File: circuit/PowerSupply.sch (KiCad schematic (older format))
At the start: 16 parts, among them CN1 Battery, CN2 Battery, Q1 IRLML6402, SW1 SW_SPDT, U1 NJM7805S, U2 LM3940IMP-3.3

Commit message: あってぃ！
今月中にElecrow発注したいんじゃ〜〜〜
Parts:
- D1: value PWR_LED -> PWR_LED(Red); footprint (none) -> LEDs:LED_0603
- R1: value 100k -> 100k 0.25W; footprint (none) -> Resistors_SMD:R_0603
- R2: value 10k -> 20k; footprint (none) -> Resistors_SMD:R_0805
- R3: value 2.7k -> 10k; footprint (none) -> Resistors_SMD:R_0805
- R4: footprint (none) -> Resistors_SMD:R_0603
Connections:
- net labels removed: +3V3
- wire segments 69 -> 64
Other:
- note added: "I = 2.8 / 10k \n = 0.28mA\nWu = 0.1568 W < 1/4 W\nWd = 0.0784 W < 1/4 W"
- note added: "Imax = 1.5A\n"
- note added: "Imax = 1A"
- note added: "R = (5 - 1.9)/0.005 = 620"
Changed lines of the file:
@@
 P 2400 1800
 F 0 "R1" H 2470 1846 50  0000 L CNN
-F 1 "100k" H 2470 1755 50  0000 L CNN
-F 2 "" V 2330 1800 50  0001 C CNN
+F 1 "100k 0.25W" H 2470 1755 50  0000 L CNN
+F 2 "Resistors_SMD:R_0603" V 2330 1800 50  0001 C CNN
 F 3 "" H 2400 1800 50  0001 C CNN
 	1    2400 1800
@@
 P 4750 1950
 F 0 "D1" V 4789 1833 50  0000 R CNN
-F 1 "PWR_LED" V 4698 1833 50  0000 R CNN
-F 2 "" H 4750 1950 50  0001 C CNN
-F 3 "" H 4750 1950 50  0001 C CNN
+F 1 "PWR_LED(Red)" V 4698 1833 50  0000 R CNN
+F 2 "LEDs:LED_0603" H 4750 1950 50  0001 C CNN
+F 3 "https://akizukidenshi.com/download/ds/optosupply/OSXX1608C1A_ver_a_10.pdf" H 4750 1950 50  0001 C CNN
 	1    4750 1950
 	0    -1   -1   0
@@
 F 0 "R4" H 4820 1596 50  0000 L CNN
 F 1 "1k" H 4820 1505 50  0000 L CNN
-F 2 "" V 4680 1550 50  0001 C CNN
+F 2 "Resistors_SMD:R_0603" V 4680 1550 50  0001 C CNN
 F 3 "" H 4750 1550 50  0001 C CNN
 	1    4750 1550
@@
 P 3150 3800
 F 0 "R2" H 3220 3846 50  0000 L CNN
-F 1 "10k" H 3220 3755 50  0000 L CNN
-F 2 "" V 3080 3800 50  0001 C CNN
+F 1 "20k" H 3220 3755 50  0000 L CNN
+F 2 "Resistors_SMD:R_0805" V 3080 3800 50  0001 C CNN
 F 3 "" H 3150 3800 50  0001 C CNN
 	1    3150 3800
@@
 P 3150 4300
 F 0 "R3" H 3220 4346 50  0000 L CNN
-F 1 "2.7k" H 3220 4255 50  0000 L CNN
-F 2 "" V 3080 4300 50  0001 C CNN
+F 1 "10k" H 3220 4255 50  0000 L CNN
+F 2 "Resistors_SMD:R_0805" V 3080 4300 50  0001 C CNN
 F 3 "" H 3150 4300 50  0001 C CNN
 	1    3150 4300
@@
 Wire Wire Line
 	3150 4050 3150 4150
-Text Notes 3450 3800 0    50   ~ 0
+Text Notes 3450 3550 0    50   ~ 0
 VCC=8.4V\nSEN_BAT=8.4 * 10k / (10k+20k)\n = 2.8V
 $Comp
@@
 	1    0    0    -1
 $EndComp
-$Comp
-L power:+5V #PWR0113
-U 1 1 5F96E56A
-P 2150 3500
-F 0 "#PWR0113" H 2150 3350 50  0001 C CNN
-F 1 "+5V" H 2165 3673 50  0000 C CNN
-F 2 "" H 2150 3500 50  0001 C CNN
-F 3 "" H 2150 3500 50  0001 C CNN
-	1    2150 3500
-	1    0    0    -1
-$EndComp
 Wire Wire Line
 	1150 3600 1150 3500
@@
 Wire Wire Line
 	1800 3600 1800 3500
-Wire Wire Line
-	2150 3500 2150 3600
 $Comp
 L regul:LM3940IMP-3.3 U2
@@
 L power:GND #PWR0114
 U 1 1 5F98E5D7
-P 6500 2250
-F 0 "#PWR0114" H 6500 2000 50  0001 C CNN
-F 1 "GND" H 6505 2077 50  0000 C CNN
-F 2 "" H 6500 2250 50  0001 C CNN
-F 3 "" H 6500 2250 50  0001 C CNN
-	1    6500 2250
+P 6500 2400
+F 0 "#PWR0114" H 6500 2150 50  0001 C CNN
+F 1 "GND" H 6505 2227 50  0000 C CNN
+F 2 "" H 6500 2400 50  0001 C CNN
+F 3 "" H 6500 2400 50  0001 C CNN
+	1    6500 2400
 	1    0    0    -1
 $EndComp
@@
 	7700 1250 7200 1250
 Connection ~ 7200 1250
-$Comp
-L power:+3V3 #PWR0116
-U 1 1 5F9A92FF
-P 1450 3950
-F 0 "#PWR0116" H 1450 3800 50  0001 C CNN
-F 1 "+3V3" H 1465 4123 50  0000 C CNN
-F 2 "" H 1450 3950 50  0001 C CNN
-F 3 "" H 1450 3950 50  0001 C CNN
-	1    1450 3950
-	1    0    0    -1
-$EndComp
-$Comp
-L power:PWR_FLAG #FLG0105
-U 1 1 5F9A9842
-P 1800 3950
-F 0 "#FLG0105" H 1800 4025 50  0001 C CNN
-F 1 "PWR_FLAG" H 1800 4123 50  0000 C CNN
-F 2 "" H 1800 3950 50  0001 C CNN
-F 3 "" H 1800 3950 50  0001 C CNN
-	1    1800 3950
-	1    0    0    -1
-$EndComp
-Wire Wire Line
-	1450 3950 1450 4100
-Wire Wire Line
-	1450 4100 1800 4100
-Wire Wire Line
-	1800 4100 1800 3950
 NoConn ~ 2500 2400
-$Comp
-L power:PWR_FLAG #FLG0104
-U 1 1 5F9823F2
-P 2500 3500
-F 0 "#FLG0104" H 2500 3575 50  0001 C CNN
-F 1 "PWR_FLAG" H 2500 3673 50  0000 C CNN
-F 2 "" H 2500 3500 50  0001 C CNN
-F 3 "" H 2500 3500 50  0001 C CNN
-	1    2500 3500
-	1    0    0    -1
-$EndComp
-Wire Wire Line
-	2150 3600 2500 3600
-Wire Wire Line
-	2500 3600 2500 3500
 Wire Wire Line
 	2750 1000 2750 1250
 $Comp
-L power:+3.3V #PWR?
+L power:+3.3V #PWR0131
 U 1 1 5F9CE132
 P 7700 1000
-F 0 "#PWR?" H 7700 850 50  0001 C CNN
+F 0 "#PWR0131" H 7700 850 50  0001 C CNN
 F 1 "+3.3V" H 7715 1173 50  0000 C CNN
 F 2 "" H 7700 1000 50  0001 C CNN
@@
 Text HLabel 3750 4050 2    50   Input ~ 0
 BAT_MONI
+Text Notes 3900 1100 0    50   ~ 0
+Imax = 1.5A\n
+Text Notes 6650 1000 0    50   ~ 0
+Imax = 1A
+Wire Wire Line
+	6500 2250 6500 2400
+Text Notes 4300 2550 0    50   ~ 0
+R = (5 - 1.9)/0.005 = 620
+Text Notes 2050 4150 0    50   ~ 0
+I = 2.8 / 10k \n  = 0.28mA\nWu = 0.1568 W < 1/4 W\nWd = 0.0784 W < 1/4 W
 $EndSCHEMATC

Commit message: Kicad v5.1.8対応
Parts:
- removed C5: 33uF, symbol device:C
- removed U2: LM3940IMP-3.3, TO_SOT_Packages_SMD:SOT-223, symbol regul:LM3940IMP-3.3
- added C24: 2.2u, symbol Device:C
- added U4: ADP7182AUJZ-3.3, Package_TO_SOT_SMD:TSOT-23-5, symbol Regulator_Linear:ADP7182AUJZ-3.3
- C1: value 0.33uF -> 4.7u; footprint (none) -> Capacitors_SMD:C_0805; symbol device:C -> Device:C
- C2: symbol device:C -> Device:C
- C3: value 0.1uF -> 1u; footprint (none) -> Capacitors_SMD:C_0603; symbol device:C -> Device:C
- C4: value 0.47uF -> 2.2u; symbol device:C -> Device:C
- CN1, CN2: symbol conn:Conn_01x02 -> Connector_Generic:Conn_01x02
- D1: symbol device:LED -> Device:LED
- Q1: symbol device:Q_PMOS_GSD -> Device:Q_PMOS_GSD
- R1, R2, R3, R4: symbol device:R -> Device:R
- SW1: symbol switches:SW_SPDT -> Switch:SW_SPDT
- U1: symbol regul:NJM7805S -> Regulator_Linear:NJM7805S
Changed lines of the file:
@@
 $EndComp
 $Comp
-L device:R R1
+L Device:R R1
 U 1 1 5F95E89C
 P 2400 1800
@@
 $EndComp
 $Comp
-L conn:Conn_01x02 CN1
+L Connector_Generic:Conn_01x02 CN1
 U 1 1 5F9556B5
 P 1000 1350
+AR Path="/5F9556B5" Ref="CN1"  Part="1"
+AR Path="/5F951566/5F9556B5" Ref="CN1"  Part="1"
 F 0 "CN1" H 1000 1000 50  0000 C CNN
 F 1 "Battery" H 1000 1100 50  0000 C CNN
@@
 Connection ~ 1750 1250
 $Comp
-L conn:Conn_01x02 CN2
+L Connector_Generic:Conn_01x02 CN2
 U 1 1 5F93F701
 P 1000 1900
+AR Path="/5F93F701" Ref="CN2"  Part="1"
+AR Path="/5F951566/5F93F701" Ref="CN2"  Part="1"
 F 0 "CN2" H 1000 1550 50  0000 C CNN
 F 1 "Battery" H 1000 1650 50  0000 C CNN
@@
 $EndComp
 $Comp
-L device:Q_PMOS_GSD Q1
+L Device:Q_PMOS_GSD Q1
 U 1 1 5F95A78B
 P 2400 1350
@@
 Connection ~ 2400 1600
 $Comp
-L switches:SW_SPDT SW1
+L Switch:SW_SPDT SW1
 U 1 1 5F987A18
 P 2400 2200
@@
 	2400 2000 2400 1950
 $Comp
-L device:LED D1
+L Device:LED D1
 U 1 1 5F94B7CC
 P 4750 1950
@@
 	4750 2100 4750 2200
 $Comp
-L regul:NJM7805S U1
-U 1 1 5F93E0A1
-P 3600 1250
-F 0 "U1" H 3600 1565 50  0000 C CNN
-F 1 "NJM7805S" H 3600 1474 50  0000 C CNN
-F 2 "TO_SOT_Packages_SMD:TO-252-2" H 3600 1700 50  0001 C CNN
-F 3 "https://akizukidenshi.com/download/ds/njr/NJM7800S_J.pdf" H 3650 950 50  0001 C CNN
-	1    3600 1250
-	1    0    0    -1
-$EndComp
-$Comp
 L power:GND #PWR0106
 U 1 1 5F9424A0
@@
 Wire Wire Line
 	3600 1600 3600 1750
-$Comp
-L device:C C1
-U 1 1 5F942D36
-P 3100 1550
-F 0 "C1" H 3215 1596 50  0000 L CNN
-F 1 "0.33uF" H 3215 1505 50  0000 L CNN
-F 2 "" H 3138 1400 50  0001 C CNN
-F 3 "" H 3100 1550 50  0001 C CNN
-	1    3100 1550
-	1    0    0    -1
-$EndComp
 Wire Wire Line
 	2750 1250 3100 1250
@@
 Wire Wire Line
 	3600 1750 3600 1800
-$Comp
-L device:C C3
-U 1 1 5F943C3B
-P 4100 1550
-F 0 "C3" H 4215 1596 50  0000 L CNN
-F 1 "0.1uF" H 4215 1505 50  0000 L CNN
-F 2 "" H 4138 1400 50  0001 C CNN
-F 3 "" H 4100 1550 50  0001 C CNN
-	1    4100 1550
-	1    0    0    -1
-$EndComp
 Wire Wire Line
 	3600 1750 4100 1750
@@
 	4100 1250 4100 1400
 $Comp
-L device:R R4
+L Device:R R4
 U 1 1 5F945E92
 P 4750 1550
@@
 $EndComp
 $Comp
-L device:R R2
+L Device:R R2
 U 1 1 5F95A42B
 P 3150 3800
@@
 $EndComp
 $Comp
-L device:R R3
+L Device:R R3
 U 1 1 5F95A966
 P 3150 4300
@@
 VCC=8.4V\nSEN_BAT=8.4 * 10k / (10k+20k)\n = 2.8V
 $Comp
-L device:C C2
+L Device:C C2
 U 1 1 5F95E36D
 P 3550 4300
@@
 	1800 3600 1800 3500
 $Comp
-L regul:LM3940IMP-3.3 U2
-U 1 1 5F98DB71
-P 6500 1350
-F 0 "U2" H 6500 1715 50  0000 C CNN
-F 1 "LM3940IMP-3.3" H 6500 1624 50  0000 C CNN
-F 2 "TO_SOT_Packages_SMD:SOT-223" H 6500 1700 50  0001 C CNN
-F 3 "https://www.ti.com/lit/ds/symlink/lm3940.pdf?HQS=TI-null-null-digikeymode-df-pf-null-wwe&ts=1603528827635" H 6500 1700 50  0001 C CNN
-	1    6500 1350
-	1    0    0    -1
-$EndComp
-$Comp
 L power:GND #PWR0114
 U 1 1 5F98E5D7
-P 6500 2400
-F 0 "#PWR0114" H 6500 2150 50  0001 C CNN
-F 1 "GND" H 6505 2227 50  0000 C CNN
-F 2 "" H 6500 2400 50  0001 C CNN
-F 3 "" H 6500 2400 50  0001 C CNN
-	1    6500 2400
-	1    0    0    -1
-$EndComp
-Wire Wire Line
-	6000 1450 6000 2250
-Wire Wire Line
-	6000 2250 6500 2250
-Wire Wire Line
-	7000 1450 7000 2250
-Wire Wire Line
-	7000 2250 6500 2250
-Connection ~ 6500 2250
-Wire Wire Line
-	6000 1250 5600 1250
-$Comp
-L device:C C4
-U 1 1 5F992186
-P 5600 1800
-F 0 "C4" H 5715 1846 50  0000 L CNN
-F 1 "0.47uF" H 5715 1755 50  0000 L CNN
-F 2 "" H 5638 1650 50  0001 C CNN
-F 3 "" H 5600 1800 50  0001 C CNN
-	1    5600 1800
-	1    0    0    -1
-$EndComp
-Wire Wire Line
-	5600 1250 5600 1650
-Connection ~ 5600 1250
-Wire Wire Line
-	5600 1250 4750 1250
-Wire Wire Line
-	5600 1950 5600 2250
-Wire Wire Line
-	5600 2250 6000 2250
-Connection ~ 6000 2250
-$Comp
-L device:C C5
-U 1 1 5F99CDC1
-P 7200 1800
-F 0 "C5" H 7315 1846 50  0000 L CNN
-F 1 "33uF" H 7315 1755 50  0000 L CNN
-F 2 "" H 7238 1650 50  0001 C CNN
-F 3 "" H 7200 1800 50  0001 C CNN
-	1    7200 1800
-	1    0    0    -1
-$EndComp
-Wire Wire Line
-	7200 1950 7200 2250
-Wire Wire Line
-	7200 2250 7000 2250
-Connection ~ 7000 2250
-Wire Wire Line
-	7000 1250 7200 1250
-Wire Wire Line
-	7200 1250 7200 1650
+P 6500 2250
+F 0 "#PWR0114" H 6500 2000 50  0001 C CNN
+F 1 "GND" H 6505 2077 50  0000 C CNN
+F 2 "" H 6500 2250 50  0001 C CNN
+F 3 "" H 6500 2250 50  0001 C CNN
+	1    6500 2250
+	1    0    0    -1
+$EndComp
+Connection ~ 6500 2100
+Wire Wire Line
+	5850 1250 5850 1650
+Connection ~ 5850 1250
+Wire Wire Line
+	5850 1250 4750 1250
+Wire Wire Line
+	5850 1950 5850 2100
+Wire Wire Line
+	6950 1250 6950 1650
 Wire Wire Line
 	7700 1000 7700 1250
 Wire Wire Line
-	7700 1250 7200 1250
-Connection ~ 7200 1250
+	7700 1250 6950 1250
+Connection ~ 6950 1250
 NoConn ~ 2500 2400
 Wire Wire Line
@@
 Imax = 1A
 Wire Wire Line
-	6500 2250 6500 2400
+	6500 2100 6500 2250
 Text Notes 4300 2550 0    50   ~ 0
 R = (5 - 1.9)/0.005 = 620
 Text Notes 2050 4150 0    50   ~ 0
 I = 2.8 / 10k \n  = 0.28mA\nWu = 0.1568 W < 1/4 W\nWd = 0.0784 W < 1/4 W
+$Comp
+L Device:C C4
+U 1 1 5F992186
+P 5850 1800
+F 0 "C4" H 5965 1846 50  0000 L CNN
+F 1 "2.2u" H 5965 1755 50  0000 L CNN
+F 2 "" H 5888 1650 50  0001 C CNN
+F 3 "" H 5850 1800 50  0001 C CNN
+	1    5850 1800
+	1    0    0    -1
+$EndComp
+$Comp
+L Device:C C1
+U 1 1 5F942D36
+P 3100 1550
+F 0 "C1" H 3215 1596 50  0000 L CNN
+F 1 "4.7u" H 3215 1505 50  0000 L CNN
+F 2 "Capacitors_SMD:C_0805" H 3138 1400 50  0001 C CNN
+F 3 "" H 3100 1550 50  0001 C CNN
+	1    3100 1550
+	1    0    0    -1
+$EndComp
+$Comp
+L Regulator_Linear:NJM7805S U1
+U 1 1 5F93E0A1
+P 3600 1250
+F 0 "U1" H 3600 1565 50  0000 C CNN
+F 1 "NJM7805S" H 3600 1474 50  0000 C CNN
+F 2 "TO_SOT_Packages_SMD:TO-252-2" H 3600 1700 50  0001 C CNN
+F 3 "https://akizukidenshi.com/download/ds/njr/NJM7800S_J.pdf" H 3650 950 50  0001 C CNN
+	1    3600 1250
+	1    0    0    -1
+$EndComp
+$Comp
+L Device:C C3
+U 1 1 5F943C3B
+P 4100 1550
+F 0 "C3" H 4215 1596 50  0000 L CNN
+F 1 "1u" H 4215 1505 50  0000 L CNN
+F 2 "Capacitors_SMD:C_0603" H 4138 1400 50  0001 C CNN
+F 3 "" H 4100 1550 50  0001 C CNN
+	1    4100 1550
+	1    0    0    -1
+$EndComp
+Wire Wire Line
+	5850 2100 6500 2100
+Wire Wire Line
+	6500 2100 6950 2100
+$Comp
+L Regulator_Linear:ADP7182AUJZ-3.3 U4
+U 1 1 5FB8CF9C
+P 6500 1350
+F 0 "U4" H 6500 983 50  0000 C CNN
+F 1 "ADP7182AUJZ-3.3" H 6500 1074 50  0000 C CNN
+F 2 "Package_TO_SOT_SMD:TSOT-23-5" H 6500 950 50  0001 C CIN
+F 3 "https://www.analog.com/media/en/technical-documentation/data-sheets/ADP7182.pdf" H 6500 850 50  0001 C CNN
+	1    6500 1350
+	1    0    0    1
+$EndComp
+Wire Wire Line
+	5850 1250 6000 1250
+Wire Wire Line
+	6900 1250 6950 1250
+Wire Wire Line
+	6100 1450 6000 1450
+Wire Wire Line
+	6000 1450 6000 1250
+Connection ~ 6000 1250
+Wire Wire Line
+	6000 1250 6100 1250
+Wire Wire Line
+	6500 1650 6500 2100
+$Comp
+L Device:C C24
+U 1 1 5FBA0D44
+P 6950 1800
+F 0 "C24" H 7065 1846 50  0000 L CNN
+F 1 "2.2u" H 7065 1755 50  0000 L CNN
+F 2 "" H 6988 1650 50  0001 C CNN
+F 3 "" H 6950 1800 50  0001 C CNN
+	1    6950 1800
+	1    0    0    -1
+$EndComp
+Wire Wire Line
+	6950 1950 6950 2100
 $EndSCHEMATC

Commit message: Kicadのpcbnew映らないくてキレそう
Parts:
- C2, C24, C4: footprint (none) -> Capacitors_SMD:C_0603
- CN1, CN2: footprint (none) -> Connectors_JST:JST_PH_B2B-PH-K_02x2.00mm_Straight
- Q1: footprint (none) -> TO_SOT_Packages_SMD:SOT-23
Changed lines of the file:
@@
 F 0 "CN1" H 1000 1000 50  0000 C CNN
 F 1 "Battery" H 1000 1100 50  0000 C CNN
-F 2 "" H 1000 1350 50  0001 C CNN
+F 2 "Connectors_JST:JST_PH_B2B-PH-K_02x2.00mm_Straight" H 1000 1350 50  0001 C CNN
 F 3 "~" H 1000 1350 50  0001 C CNN
 	1    1000 1350
@@
 F 0 "CN2" H 1000 1550 50  0000 C CNN
 F 1 "Battery" H 1000 1650 50  0000 C CNN
-F 2 "" H 1000 1900 50  0001 C CNN
+F 2 "Connectors_JST:JST_PH_B2B-PH-K_02x2.00mm_Straight" H 1000 1900 50  0001 C CNN
 F 3 "~" H 1000 1900 50  0001 C CNN
 	1    1000 1900
@@
 F 0 "Q1" H 2606 1396 50  0000 L CNN
 F 1 "IRLML6402" H 2606 1305 50  0000 L CNN
-F 2 "" H 2600 1450 50  0001 C CNN
-F 3 "" H 2400 1350 50  0001 C CNN
+F 2 "TO_SOT_Packages_SMD:SOT-23" H 2600 1450 50  0001 C CNN
+F 3 "https://akizukidenshi.com/download/ds/ir/irlml6402.pdf" H 2400 1350 50  0001 C CNN
 	1    2400 1350
 	0    1    -1   0
@@
 F 0 "C2" H 3665 4346 50  0000 L CNN
 F 1 "0.1uF" H 3665 4255 50  0000 L CNN
-F 2 "" H 3588 4150 50  0001 C CNN
+F 2 "Capacitors_SMD:C_0603" H 3588 4150 50  0001 C CNN
 F 3 "" H 3550 4300 50  0001 C CNN
 	1    3550 4300
@@
 F 0 "C4" H 5965 1846 50  0000 L CNN
 F 1 "2.2u" H 5965 1755 50  0000 L CNN
-F 2 "" H 5888 1650 50  0001 C CNN
+F 2 "Capacitors_SMD:C_0603" H 5888 1650 50  0001 C CNN
 F 3 "" H 5850 1800 50  0001 C CNN
 	1    5850 1800
@@
 F 0 "C24" H 7065 1846 50  0000 L CNN
 F 1 "2.2u" H 7065 1755 50  0000 L CNN
-F 2 "" H 6988 1650 50  0001 C CNN
+F 2 "Capacitors_SMD:C_0603" H 6988 1650 50  0001 C CNN
 F 3 "" H 6950 1800 50  0001 C CNN
 	1    6950 1800

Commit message: スーパーエンジニアの登竜門たる文彦は当然スーパーエンジニア
あってぃ許さない
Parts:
- C1: footprint Capacitors_SMD:C_0805 -> Capacitor_SMD:C_0805_2012Metric
- C2, C24, C3, C4: footprint Capacitors_SMD:C_0603 -> Capacitor_SMD:C_0603_1608Metric
- CN1, CN2: footprint Connectors_JST:JST_PH_B2B-PH-K_02x2.00mm_Straight -> Connector_JST:JST_PH_B2B-PH-K_1x02_P2.00mm_Vertical
- D1: footprint LEDs:LED_0603 -> LED_SMD:LED_0603_1608Metric
- Q1: footprint TO_SOT_Packages_SMD:SOT-23 -> Package_TO_SOT_SMD:SOT-23
- R1, R4: footprint Resistors_SMD:R_0603 -> Resistor_SMD:R_0603_1608Metric
- R2, R3: footprint Resistors_SMD:R_0805 -> Resistor_SMD:R_0805_2012Metric
- SW1: footprint (none) -> Button_Switch_THT:SW_CuK_JS202011CQN_DPDT_Straight
- U1: footprint TO_SOT_Packages_SMD:TO-252-2 -> Package_TO_SOT_SMD:TO-252-2; symbol Regulator_Linear:NJM7805S -> Micromouse-rescue:NJM7805S-Regulator_Linear
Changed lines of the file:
@@
 F 0 "R1" H 2470 1846 50  0000 L CNN
 F 1 "100k 0.25W" H 2470 1755 50  0000 L CNN
-F 2 "Resistors_SMD:R_0603" V 2330 1800 50  0001 C CNN
+F 2 "Resistor_SMD:R_0603_1608Metric" V 2330 1800 50  0001 C CNN
 F 3 "" H 2400 1800 50  0001 C CNN
 	1    2400 1800
@@
 F 0 "CN1" H 1000 1000 50  0000 C CNN
 F 1 "Battery" H 1000 1100 50  0000 C CNN
-F 2 "Connectors_JST:JST_PH_B2B-PH-K_02x2.00mm_Straight" H 1000 1350 50  0001 C CNN
+F 2 "Connector_JST:JST_PH_B2B-PH-K_1x02_P2.00mm_Vertical" H 1000 1350 50  0001 C CNN
 F 3 "~" H 1000 1350 50  0001 C CNN
 	1    1000 1350
@@
 F 0 "CN2" H 1000 1550 50  0000 C CNN
 F 1 "Battery" H 1000 1650 50  0000 C CNN
-F 2 "Connectors_JST:JST_PH_B2B-PH-K_02x2.00mm_Straight" H 1000 1900 50  0001 C CNN
+F 2 "Connector_JST:JST_PH_B2B-PH-K_1x02_P2.00mm_Vertical" H 1000 1900 50  0001 C CNN
 F 3 "~" H 1000 1900 50  0001 C CNN
 	1    1000 1900
@@
 F 0 "Q1" H 2606 1396 50  0000 L CNN
 F 1 "IRLML6402" H 2606 1305 50  0000 L CNN
-F 2 "TO_SOT_Packages_SMD:SOT-23" H 2600 1450 50  0001 C CNN
+F 2 "Package_TO_SOT_SMD:SOT-23" H 2600 1450 50  0001 C CNN
 F 3 "https://akizukidenshi.com/download/ds/ir/irlml6402.pdf" H 2400 1350 50  0001 C CNN
 	1    2400 1350
@@
 F 0 "SW1" V 2446 2012 50  0000 R CNN
 F 1 "SW_SPDT" V 2355 2012 50  0000 R CNN
-F 2 "" H 2400 2200 50  0001 C CNN
+F 2 "Button_Switch_THT:SW_CuK_JS202011CQN_DPDT_Straight" H 2400 2200 50  0001 C CNN
 F 3 "" H 2400 2200 50  0001 C CNN
 	1    2400 2200
@@
 F 0 "D1" V 4789 1833 50  0000 R CNN
 F 1 "PWR_LED(Red)" V 4698 1833 50  0000 R CNN
-F 2 "LEDs:LED_0603" H 4750 1950 50  0001 C CNN
+F 2 "LED_SMD:LED_0603_1608Metric" H 4750 1950 50  0001 C CNN
 F 3 "https://akizukidenshi.com/download/ds/optosupply/OSXX1608C1A_ver_a_10.pdf" H 4750 1950 50  0001 C CNN
 	1    4750 1950
@@
 F 0 "R4" H 4820 1596 50  0000 L CNN
 F 1 "1k" H 4820 1505 50  0000 L CNN
-F 2 "Resistors_SMD:R_0603" V 4680 1550 50  0001 C CNN
+F 2 "Resistor_SMD:R_0603_1608Metric" V 4680 1550 50  0001 C CNN
 F 3 "" H 4750 1550 50  0001 C CNN
 	1    4750 1550
@@
 F 0 "R2" H 3220 3846 50  0000 L CNN
 F 1 "20k" H 3220 3755 50  0000 L CNN
-F 2 "Resistors_SMD:R_0805" V 3080 3800 50  0001 C CNN
+F 2 "Resistor_SMD:R_0805_2012Metric" V 3080 3800 50  0001 C CNN
 F 3 "" H 3150 3800 50  0001 C CNN
 	1    3150 3800
@@
 F 0 "R3" H 3220 4346 50  0000 L CNN
 F 1 "10k" H 3220 4255 50  0000 L CNN
-F 2 "Resistors_SMD:R_0805" V 3080 4300 50  0001 C CNN
+F 2 "Resistor_SMD:R_0805_2012Metric" V 3080 4300 50  0001 C CNN
 F 3 "" H 3150 4300 50  0001 C CNN
 	1    3150 4300
@@
 F 0 "C2" H 3665 4346 50  0000 L CNN
 F 1 "0.1uF" H 3665 4255 50  0000 L CNN
-F 2 "Capacitors_SMD:C_0603" H 3588 4150 50  0001 C CNN
+F 2 "Capacitor_SMD:C_0603_1608Metric" H 3588 4150 50  0001 C CNN
 F 3 "" H 3550 4300 50  0001 C CNN
 	1    3550 4300
@@
 F 0 "C4" H 5965 1846 50  0000 L CNN
 F 1 "2.2u" H 5965 1755 50  0000 L CNN
-F 2 "Capacitors_SMD:C_0603" H 5888 1650 50  0001 C CNN
+F 2 "Capacitor_SMD:C_0603_1608Metric" H 5888 1650 50  0001 C CNN
 F 3 "" H 5850 1800 50  0001 C CNN
 	1    5850 1800
@@
 F 0 "C1" H 3215 1596 50  0000 L CNN
 F 1 "4.7u" H 3215 1505 50  0000 L CNN
-F 2 "Capacitors_SMD:C_0805" H 3138 1400 50  0001 C CNN
+F 2 "Capacitor_SMD:C_0805_2012Metric" H 3138 1400 50  0001 C CNN
 F 3 "" H 3100 1550 50  0001 C CNN
 	1    3100 1550
@@
 $EndComp
 $Comp
-L Regulator_Linear:NJM7805S U1
+L Micromouse-rescue:NJM7805S-Regulator_Linear U1
 U 1 1 5F93E0A1
 P 3600 1250
+AR Path="/5F93E0A1" Ref="U1"  Part="1"
+AR Path="/5F951566/5F93E0A1" Ref="U1"  Part="1"
 F 0 "U1" H 3600 1565 50  0000 C CNN
 F 1 "NJM7805S" H 3600 1474 50  0000 C CNN
-F 2 "TO_SOT_Packages_SMD:TO-252-2" H 3600 1700 50  0001 C CNN
+F 2 "Package_TO_SOT_SMD:TO-252-2" H 3600 1700 50  0001 C CNN
 F 3 "https://akizukidenshi.com/download/ds/njr/NJM7800S_J.pdf" H 3650 950 50  0001 C CNN
 	1    3600 1250
@@
 F 0 "C3" H 4215 1596 50  0000 L CNN
 F 1 "1u" H 4215 1505 50  0000 L CNN
-F 2 "Capacitors_SMD:C_0603" H 4138 1400 50  0001 C CNN
+F 2 "Capacitor_SMD:C_0603_1608Metric" H 4138 1400 50  0001 C CNN
 F 3 "" H 4100 1550 50  0001 C CNN
 	1    4100 1550
@@
 F 0 "C24" H 7065 1846 50  0000 L CNN
 F 1 "2.2u" H 7065 1755 50  0000 L CNN
-F 2 "Capacitors_SMD:C_0603" H 6988 1650 50  0001 C CNN
+F 2 "Capacitor_SMD:C_0603_1608Metric" H 6988 1650 50  0001 C CNN
 F 3 "" H 6950 1800 50  0001 C CNN
 	1    6950 1800

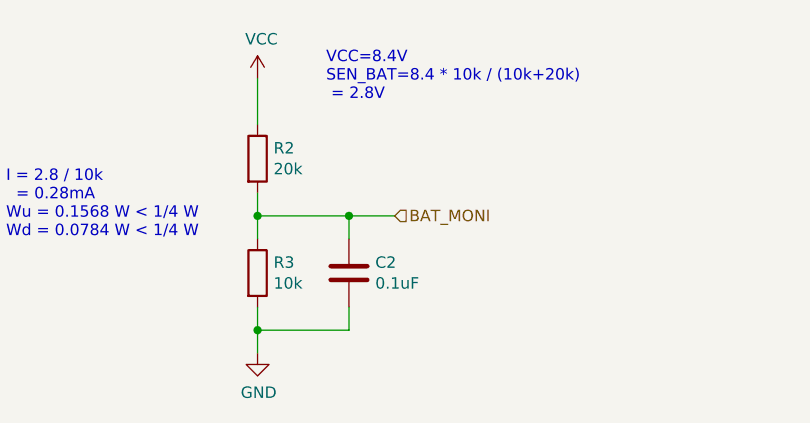
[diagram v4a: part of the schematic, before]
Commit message: Buttonクラス追加，ICM20602クラスOffset関数定義（未実装）
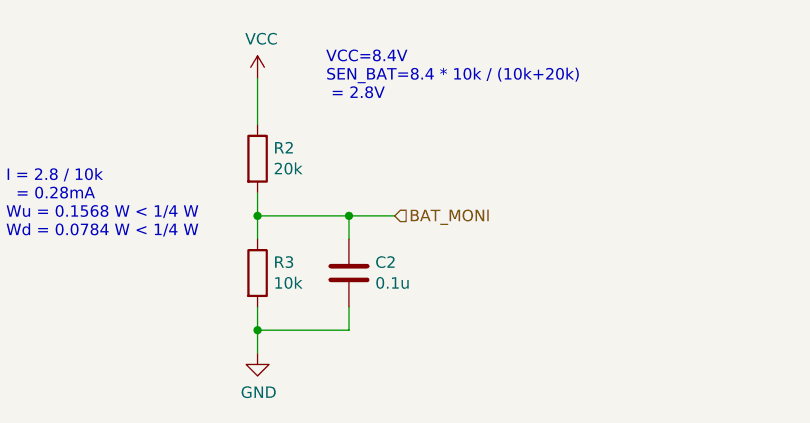
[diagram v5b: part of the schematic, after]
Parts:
- C2: value 0.1uF -> 0.1u
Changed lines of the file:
@@
 P 3550 4300
 F 0 "C2" H 3665 4346 50  0000 L CNN
-F 1 "0.1uF" H 3665 4255 50  0000 L CNN
+F 1 "0.1u" H 3665 4255 50  0000 L CNN
 F 2 "Capacitor_SMD:C_0603_1608Metric" H 3588 4150 50  0001 C CNN
 F 3 "" H 3550 4300 50  0001 C CNN
